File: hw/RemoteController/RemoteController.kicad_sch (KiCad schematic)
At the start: 27 parts, among them SW1 SW_Push, SW2 SW_SPDT, U1 nRF52810-QCxx, U2 TPS562200, Y4 13.56 MHz

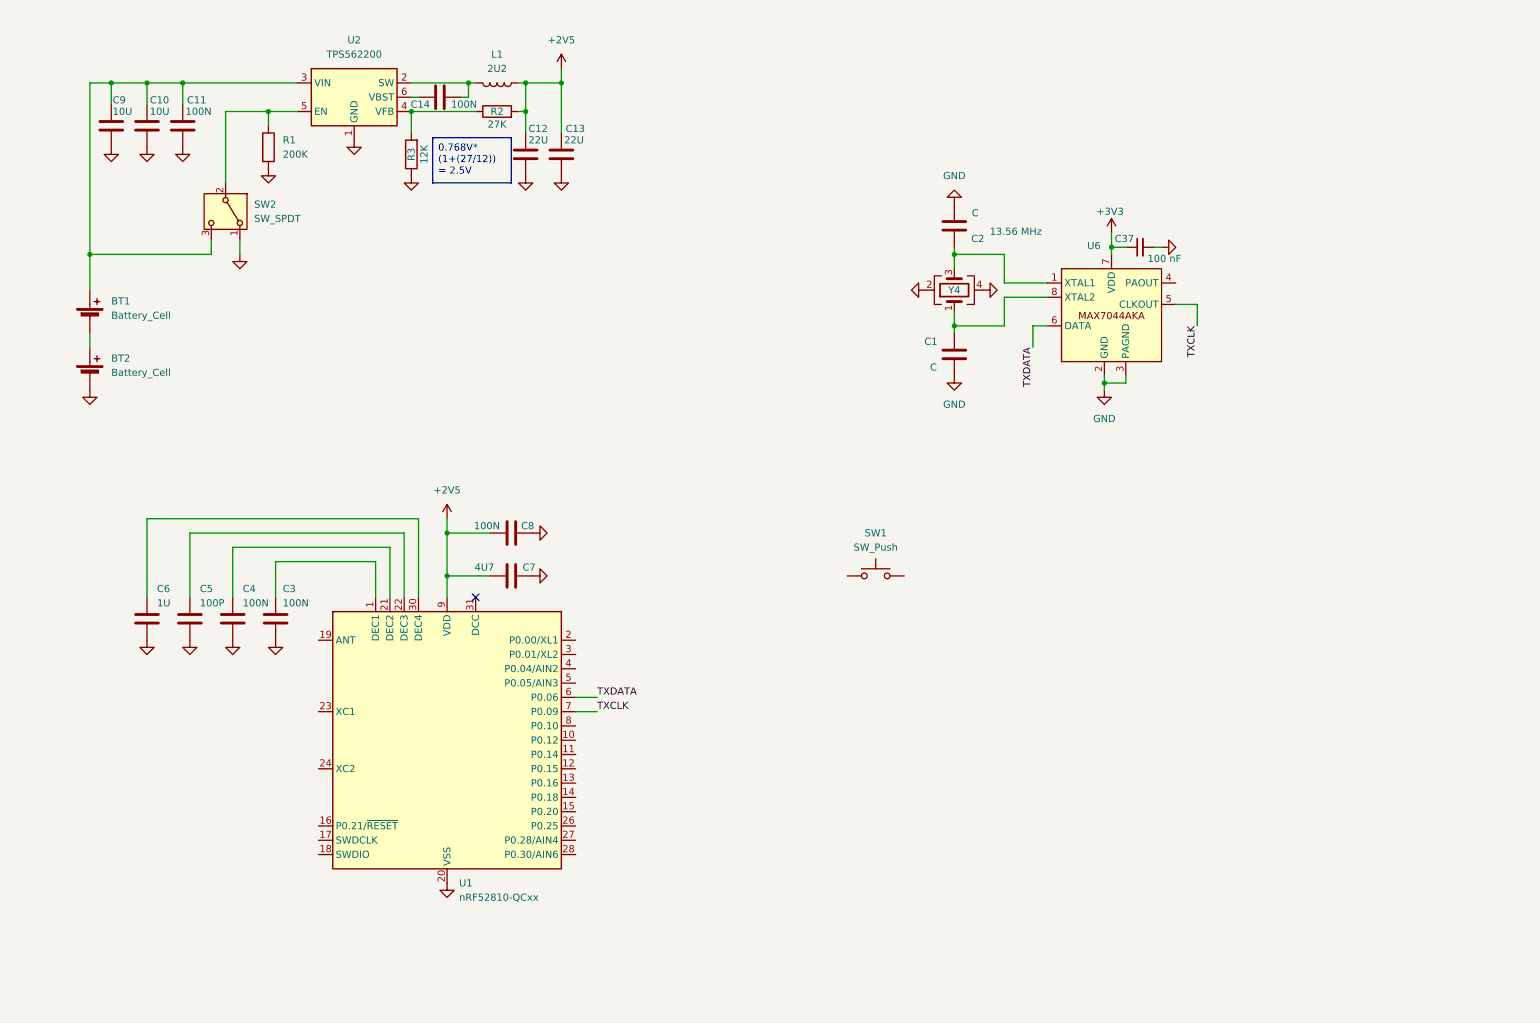
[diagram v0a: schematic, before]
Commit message: remote_ctrl: add radio and change mcu
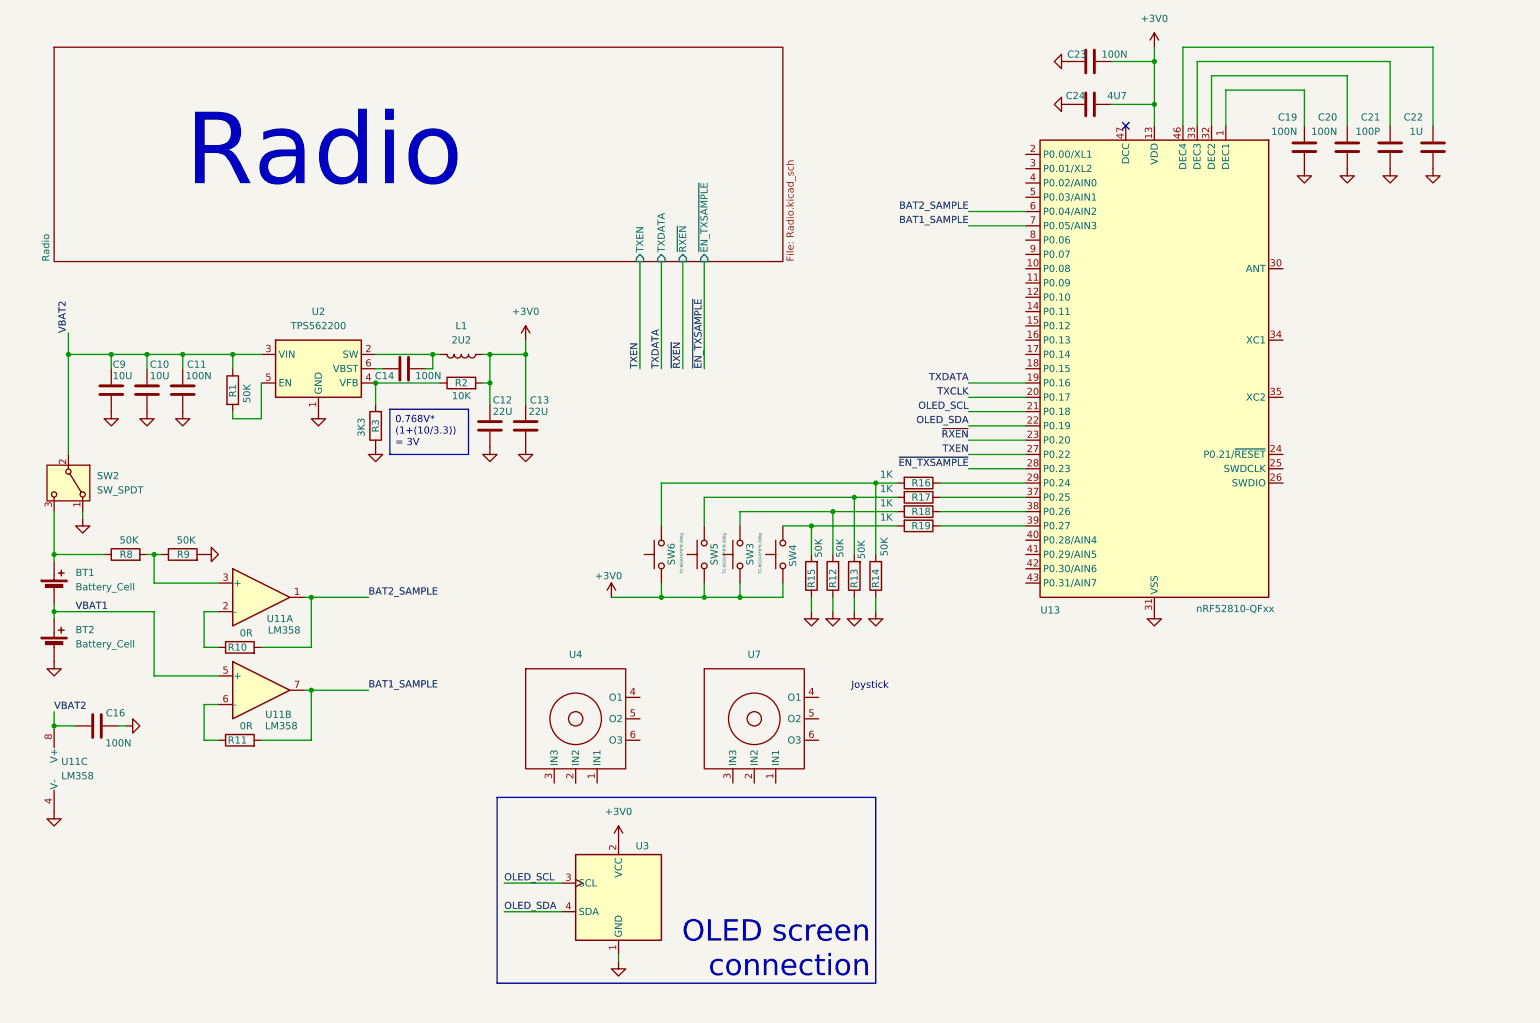
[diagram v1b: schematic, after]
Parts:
- removed C1, C2: C, Capacitor_SMD:C_0603_1608Metric_Pad1.08x0.95mm_HandSolder, symbol Device:C
- removed C3, C4, C8: 100N, Capacitor_SMD:C_0603_1608Metric_Pad1.08x0.95mm_HandSolder, symbol Device:C
- removed C37: 100 nF, Capacitor_SMD:C_0603_1608Metric_Pad1.08x0.95mm_HandSolder, symbol Device:C_Small
- removed C5: 100P, Capacitor_SMD:C_0603_1608Metric_Pad1.08x0.95mm_HandSolder, symbol Device:C
- removed C6: 1U, Capacitor_SMD:C_0603_1608Metric_Pad1.08x0.95mm_HandSolder, symbol Device:C
- removed C7: 4U7, Capacitor_SMD:C_0603_1608Metric_Pad1.08x0.95mm_HandSolder, symbol Device:C
- removed SW1: SW_Push, symbol Switch:SW_Push
- removed U1: nRF52810-QCxx, Package_DFN_QFN:QFN-32-1EP_5x5mm_P0.5mm_EP3.1x3.1mm, symbol MCU_Nordic:nRF52810-QCxx
- removed U6: (no value), steew:MAX7044AKA, symbol steew:MAX7044AKA
- removed Y4: 13.56 MHz, Crystal:Crystal_SMD_2016-4Pin_2.0x1.6mm, symbol Device:Crystal_GND24
- added C16, C19, C20, C23: 100N, Capacitor_SMD:C_0603_1608Metric_Pad1.08x0.95mm_HandSolder, symbol Device:C
- added C21: 100P, Capacitor_SMD:C_0603_1608Metric_Pad1.08x0.95mm_HandSolder, symbol Device:C
- added C22: 1U, Capacitor_SMD:C_0603_1608Metric_Pad1.08x0.95mm_HandSolder, symbol Device:C
- added C24: 4U7, Capacitor_SMD:C_0603_1608Metric_Pad1.08x0.95mm_HandSolder, symbol Device:C
- added R10, R11: 0R, Resistor_SMD:R_0603_1608Metric_Pad0.98x0.95mm_HandSolder, symbol Device:R
- added R12, R13, R14, R15, R8, R9: 50K, Resistor_SMD:R_0603_1608Metric_Pad0.98x0.95mm_HandSolder, symbol Device:R
- added R16, R17, R18, R19: 1K, Resistor_SMD:R_0603_1608Metric_Pad0.98x0.95mm_HandSolder, symbol Device:R
- added SW3, SW4, SW5, SW6: TC-6610-6*6*8-300g, Button_Switch_THT:SW_TH_Tactile_Omron_B3F-106x, symbol Switch:SW_Push
- added U11: LM358, Package_SO:SOIC-8_3.9x4.9mm_P1.27mm, symbol Amplifier_Operational:LM358
- added U13: nRF52810-QFxx, Package_DFN_QFN:QFN-48-1EP_6x6mm_P0.4mm_EP4.2x4.2mm, symbol MCU_Nordic:nRF52810-QFxx
- added U3: ER_OLEDM0.91_1x-I2C, Display:ER_OLEDM0.91_1x-I2C, symbol Display_Graphic:ER_OLEDM0.91_1x-I2C
- added U4, U7: (no value), symbol steew:YG16-FL7.8-B10Ka(80)-R
- C10, C11, C12, C13, C14, C9, L1: KiLib_Generator (none) -> SMD_2terminal_chip_molded
- R1: value 200K -> 50K; KiLib_Generator (none) -> SMD_2terminal_chip_molded
- R2: value 27K -> 10K; KiLib_Generator (none) -> SMD_2terminal_chip_molded
- R3: value 12K -> 3K3; KiLib_Generator (none) -> SMD_2terminal_chip_molded
- U2: KiLib_Generator (none) -> package/gullwing
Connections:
- net GND: now also C16.2, C19.2, C20.2, C21.2, C22.2, C23.2, C24.2, R12.1, R13.1, R14.1, R15.1, R9.2, U11.4 (V-), U13.31 (VSS), U13.45 (VSS), U13.49 (VSS), U3.1 (GND); no longer R1.2
- net TXCLK: now also U13.20 (P0.17)
- net TXDATA: now also U13.19 (P0.16)
- net VBAT2: now reaches C10.1, C11.1, C9.1, U2.3 (VIN)
- net VBAT2: now also R1.1, SW2.2 (B), C16.1, U11.8 (V+); no longer BT1.1 (+), SW2.3 (C)
- net VBAT1: now reaches BT1.2 (-), BT2.1 (+)
- net VBAT1: now also U11.5 (+)
- net +2V5 renamed +3V0
- net +3V0: now also C23.1, C24.1, SW3.1, SW4.1, SW5.1, SW6.1, U13.13 (VDD), U13.36 (VDD), U13.48 (VDD), U3.2 (VCC)
- new net: C21.1, U13.33 (DEC3)
- new net: R14.2, R16.2, SW6.2
- new net: R1.2, U2.5 (EN)
- new net: BT1.1 (+), R8.1, SW2.3 (C)
- new net: R8.2, R9.1, U11.3 (+)
- new net: R18.1, U13.38 (P0.26)
- new net: R12.2, R18.2, SW3.2
- new net: R13.2, R17.2, SW5.2
- new net: R11.1, U11.6 (-)
- new net: C19.1, U13.1 (DEC1)
- new net: R16.1, U13.29 (P0.24)
- new net: C20.1, U13.32 (DEC2)
- new net: R17.1, U13.37 (P0.25)
- new net: R19.1, U13.39 (P0.27)
- new net: C22.1, U13.46 (DEC4)
- new net: R15.2, R19.2, SW4.2
- new net: R10.1, U11.2 (-)
- new net BAT1_SAMPLE: R11.2, U11.7, U13.7 (P0.05/AIN3)
- new net BAT2_SAMPLE: R10.2, U11.1, U13.6 (P0.04/AIN2)
- new net OLED_SCL: U13.21 (P0.18), U3.3 (SCL)
- new net OLED_SDA: U13.22 (P0.19), U3.4 (SDA)
- new net TXEN: U13.27 (P0.22)
- new net ~{EN_TXSAMPLE}: U13.28 (P0.23)
- new net ~{RXEN}: U13.23 (P0.20)
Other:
- added sheet Radio (Radio.kicad_sch)
- note added: "Joystick"
- note added: "Radio"
- moved on the sheet: BT1, BT2, C10, C11, C12, C13, C14, C9, L1, R1, R2, R3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

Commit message: remote_ctrl: finish schematic
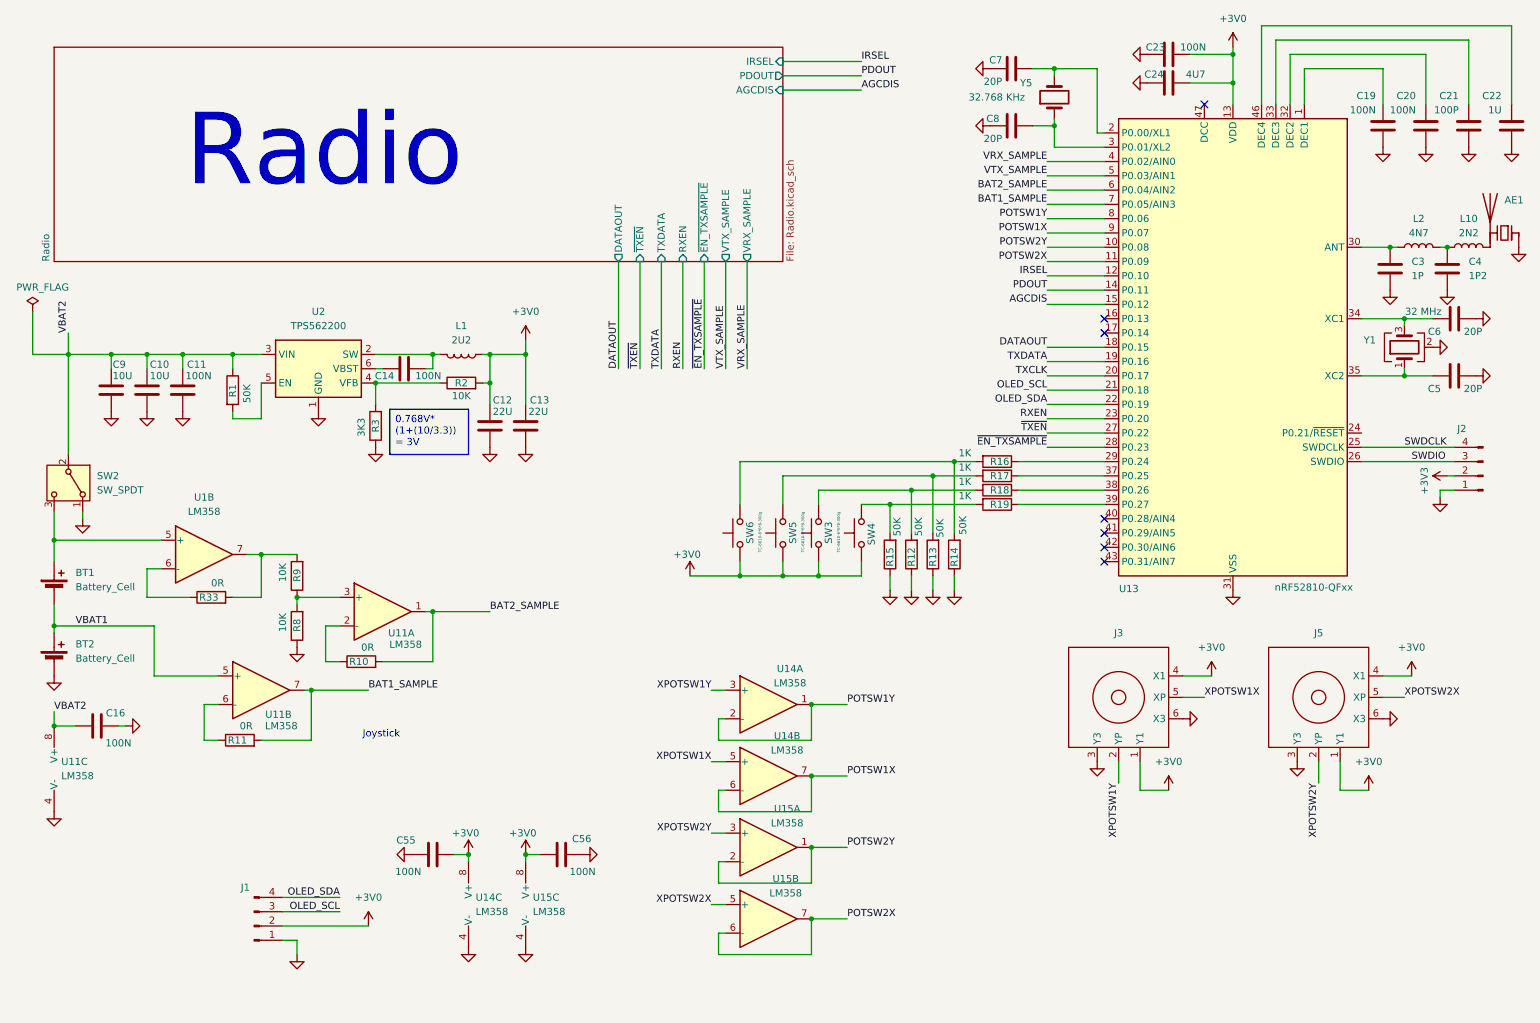
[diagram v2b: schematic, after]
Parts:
- removed U3: ER_OLEDM0.91_1x-I2C, Display:ER_OLEDM0.91_1x-I2C, symbol Display_Graphic:ER_OLEDM0.91_1x-I2C
- removed U4, U7: (no value), symbol steew:YG16-FL7.8-B10Ka(80)-R
- added AE1: Antenna_Chip, Inductor_SMD:L_1206_3216Metric_Pad1.22x1.90mm_HandSolder, symbol Device:Antenna_Chip
- added C3: 1P, Capacitor_SMD:C_0603_1608Metric_Pad1.08x0.95mm_HandSolder, symbol Device:C
- added C4: 1P2, Capacitor_SMD:C_0603_1608Metric_Pad1.08x0.95mm_HandSolder, symbol Device:C
- added C5, C6, C7, C8: 20P, Capacitor_SMD:C_0603_1608Metric_Pad1.08x0.95mm_HandSolder, symbol Device:C
- added C55, C56: 100N, Capacitor_SMD:C_0603_1608Metric_Pad1.08x0.95mm_HandSolder, symbol Device:C
- added J1: Conn_01x04_Pin, Connector_PinSocket_2.54mm:PinSocket_1x04_P2.54mm_Horizontal, symbol Connector:Conn_01x04_Pin
- added J2: Conn_01x04_Pin, Connector_JST:JST_PH_B4B-PH-K_1x04_P2.00mm_Vertical, symbol Connector:Conn_01x04_Pin
- added J3, J5: (no value), steew:YG16-FL7.8-B10Ka(80)-R, symbol steew:YG16-FL7.8-B10Ka(80)-R
- added L10: 2N2, Inductor_SMD:L_0603_1608Metric_Pad1.05x0.95mm_HandSolder, symbol Device:L
- added L2: 4N7, Inductor_SMD:L_0603_1608Metric_Pad1.05x0.95mm_HandSolder, symbol Device:L
- added R33: 0R, Resistor_SMD:R_0603_1608Metric_Pad0.98x0.95mm_HandSolder, symbol Device:R
- added U1, U14, U15: LM358, Package_SO:SOIC-8_3.9x4.9mm_P1.27mm, symbol Amplifier_Operational:LM358
- added Y1: 32 MHz, Crystal:Crystal_SMD_3225-4Pin_3.2x2.5mm_HandSoldering, symbol Device:Crystal_GND24
- added Y5: 32.768 KHz, Crystal:Crystal_SMD_3215-2Pin_3.2x1.5mm, symbol Device:Crystal
- R8, R9: value 50K -> 10K
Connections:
- net +3V0: now also C55.2, C56.1, J1.2 (Pin_2), J3.1 (Y1), J3.4 (X1), J5.1 (Y1), J5.4 (X1), U14.8 (V+), U15.8 (V+)
- net GND: now also R8.1, AE1.1 (FEED), C3.2, C4.2, C5.2, C55.1, C56.2, C6.2, C7.2, C8.2, J1.1 (Pin_1), J2.1 (Pin_1), J3.3 (Y3), J3.6 (X3), J5.3 (Y3), J5.6 (X3), U14.4 (V-), U15.4 (V-), Y1.2 (G), Y1.4 (G); no longer R9.2
- net OLED_SCL: now also J1.3 (Pin_3)
- net OLED_SDA: now also J1.4 (Pin_4)
- net at BT1.1 (+), SW2.3 (C): now also U1.5 (+); no longer R8.1
- net POTSW2Y: now reaches U13.10 (P0.08)
- net POTSW2Y: now also U15.1, U15.2 (-)
- net POTSW2X: now reaches U13.11 (P0.09)
- net POTSW2X: now also U15.6 (-), U15.7
- net IRSEL: now reaches U13.12 (P0.10)
- net PDOUT: now reaches U13.14 (P0.11)
- net AGCDIS: now reaches U13.15 (P0.12)
- net DATAOUT: now reaches U13.18 (P0.15)
- net at U13.2 (P0.00/XL1): now also C7.1, Y5.2
- net SWDCLK: now reaches U13.25 (SWDCLK)
- net SWDCLK: now also J2.4 (Pin_4)
- net SWDIO: now reaches U13.26 (SWDIO)
- net SWDIO: now also J2.3 (Pin_3)
- net at U13.3 (P0.01/XL2): now also C8.1, Y5.1
- net at U13.30 (ANT): now also C3.1, L2.1
- net at U13.34 (XC1): now also C6.1, Y1.3
- net at U13.35 (XC2): now also C5.1, Y1.1
- net VRX_SAMPLE: now reaches U13.4 (P0.02/AIN0)
- net VTX_SAMPLE: now reaches U13.5 (P0.03/AIN1)
- net POTSW1Y: now reaches U13.8 (P0.06)
- net POTSW1Y: now also U14.1, U14.2 (-)
- net POTSW1X: now reaches U13.9 (P0.07)
- net POTSW1X: now also U14.6 (-), U14.7
- net TXEN renamed ~{TXEN}
- net ~{RXEN} renamed RXEN
- new net: R33.1, U1.6 (-)
- new net: R33.2, R9.2, U1.7
- new net: AE1.2 (PCB_Trace), L10.2
- new net: C4.1, L10.1, L2.2
- new net +3V3: J2.2 (Pin_2)
- new net XPOTSW1X: J3.5 (XP), U14.5 (+)
- new net XPOTSW1Y: J3.2 (YP), U14.3 (+)
- new net XPOTSW2X: J5.5 (XP), U15.5 (+)
- new net XPOTSW2Y: J5.2 (YP), U15.3 (+)
- no-connect marks 1 -> 7
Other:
- sheet Radio ports: added AGCDIS, DATAOUT, IRSEL, PDOUT, RXEN, VRX_SAMPLE, VTX_SAMPLE, ~{TXEN}; removed TXEN, ~{RXEN}
- moved on the sheet: BT2, C19, C20, C21, C22, C23, C24, R10, R12, R13, R14, R15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

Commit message: remote_ctrl: basic PCB shape
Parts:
- added H1, H2, H3, H4: MountingHole, MountingHole:MountingHole_2.2mm_M2, symbol Mechanical:MountingHole
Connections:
- net +3V3 is gone; now on net +3V0: J2.2 (Pin_2)
